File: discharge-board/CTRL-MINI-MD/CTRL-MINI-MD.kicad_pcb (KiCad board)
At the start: 4 copper layers, 40.6 x 20.3 mm, 22 parts, among them J1 MD-L, J2 MD-R, U1 BD50FC0FP, U2 TMC2130-LA

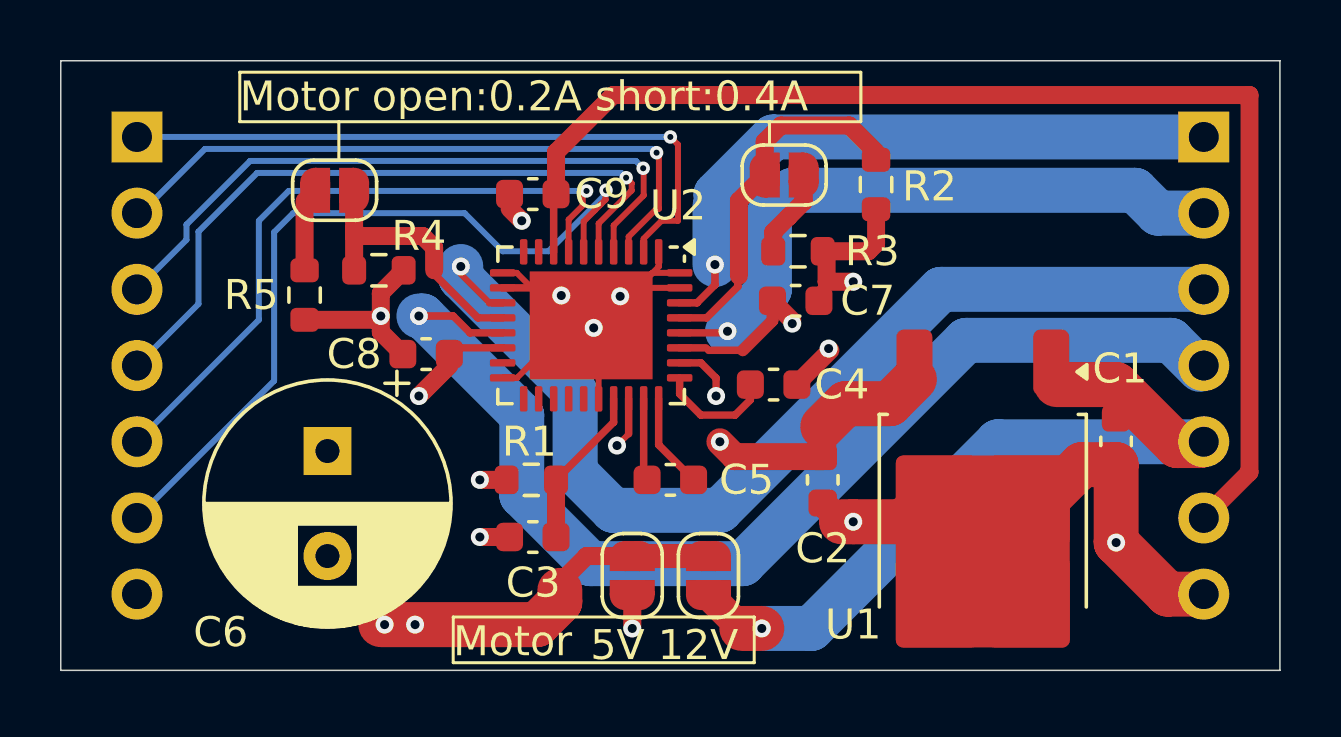
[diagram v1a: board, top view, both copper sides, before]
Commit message: Fix DFM errors
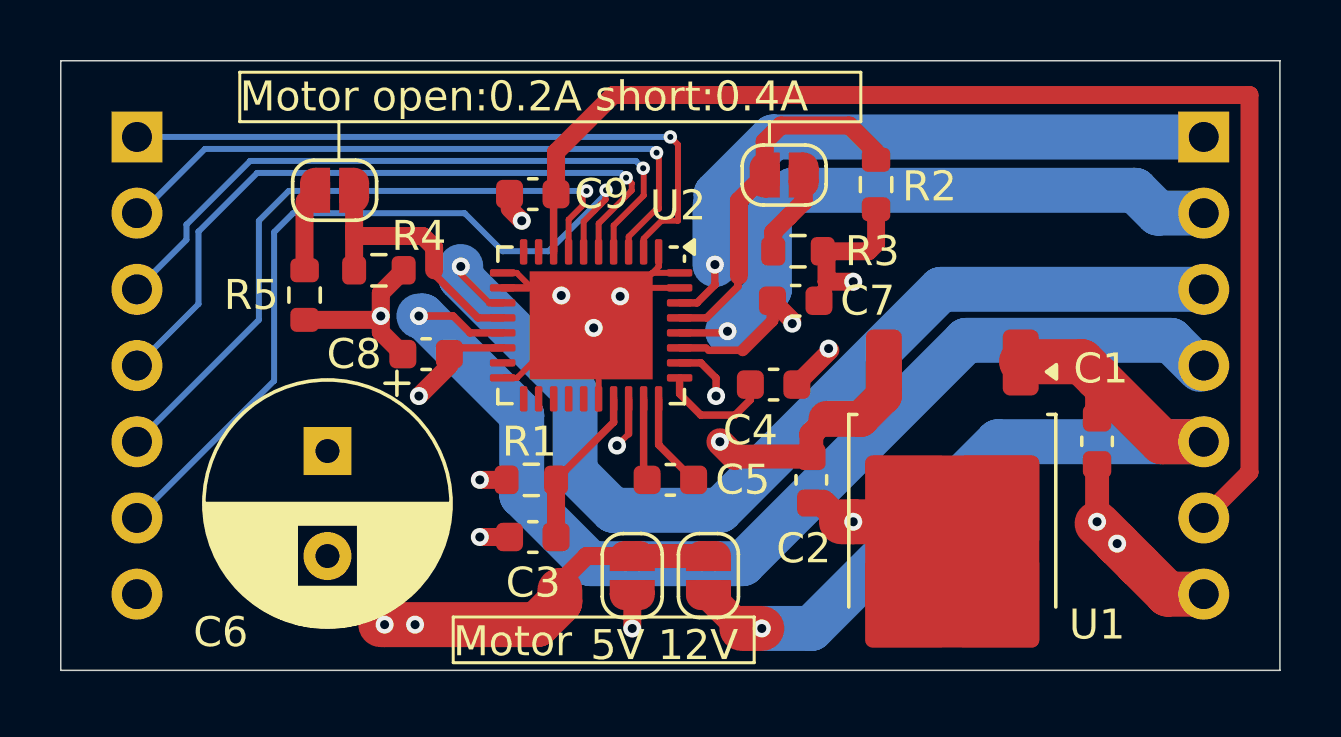
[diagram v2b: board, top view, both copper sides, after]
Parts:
- moved U1 1.02 mm to (103.4, 71.0)
- moved C1 0.64 mm to (108.2, 68.6)
- moved C2 0.38 mm to (98.7, 69.8)
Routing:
- net GND: track 49.7 -> 46.3 mm, vias 9 -> 10
- net +12V: track 25.6 -> 28.1 mm
